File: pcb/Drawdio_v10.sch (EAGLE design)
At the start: 14 parts, among them IC1 TLC551, Q1 BC327

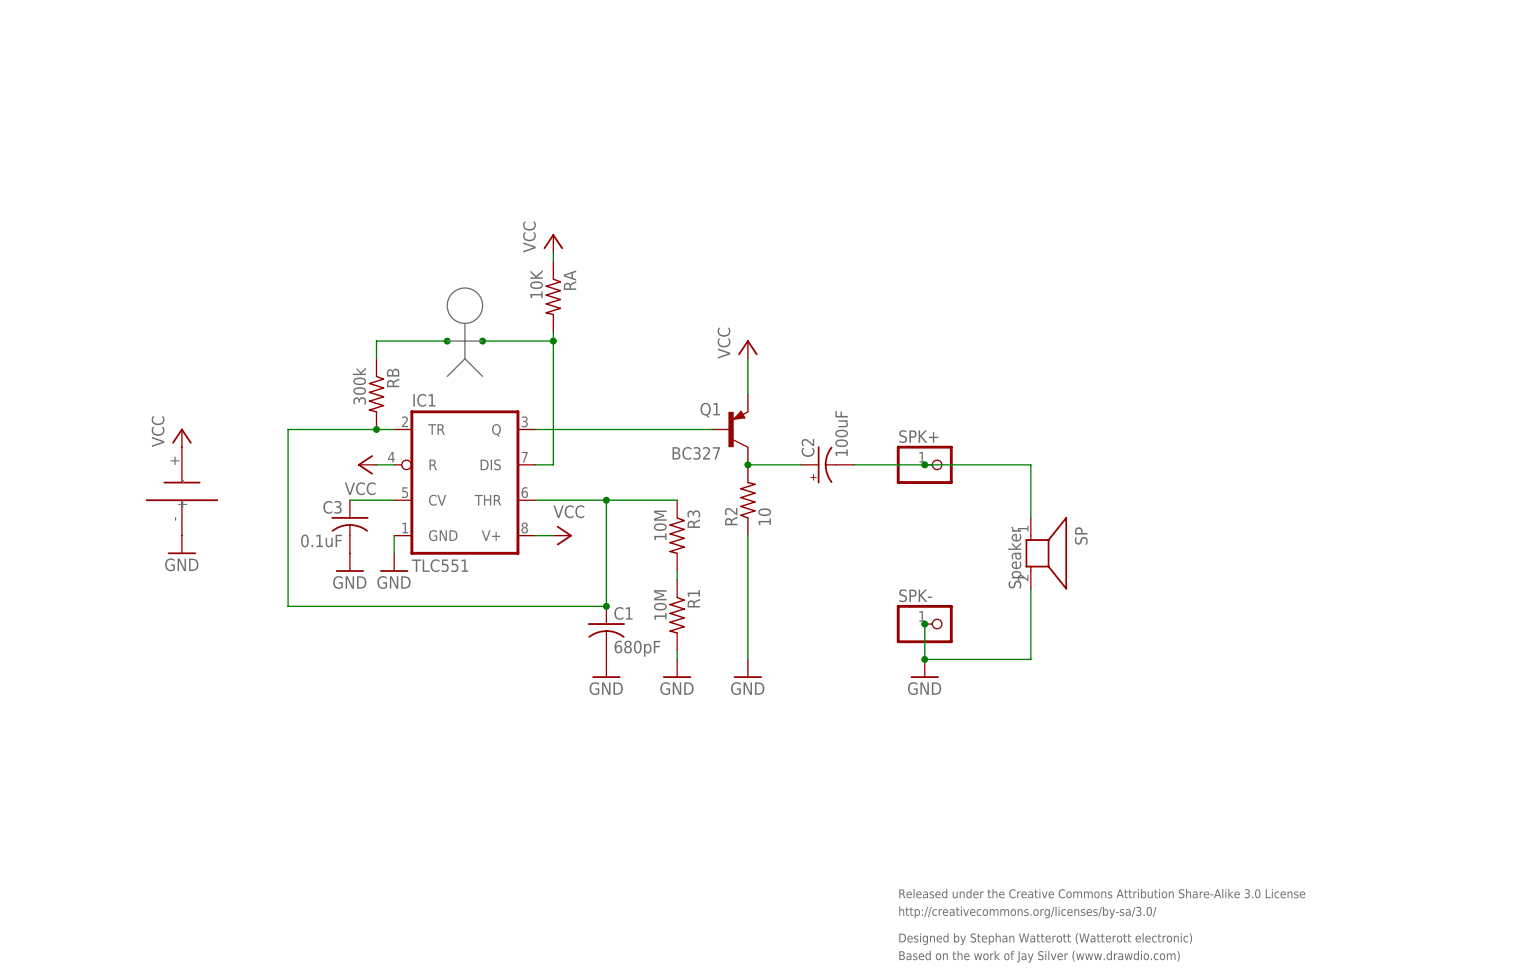
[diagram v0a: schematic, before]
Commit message: updated schematics
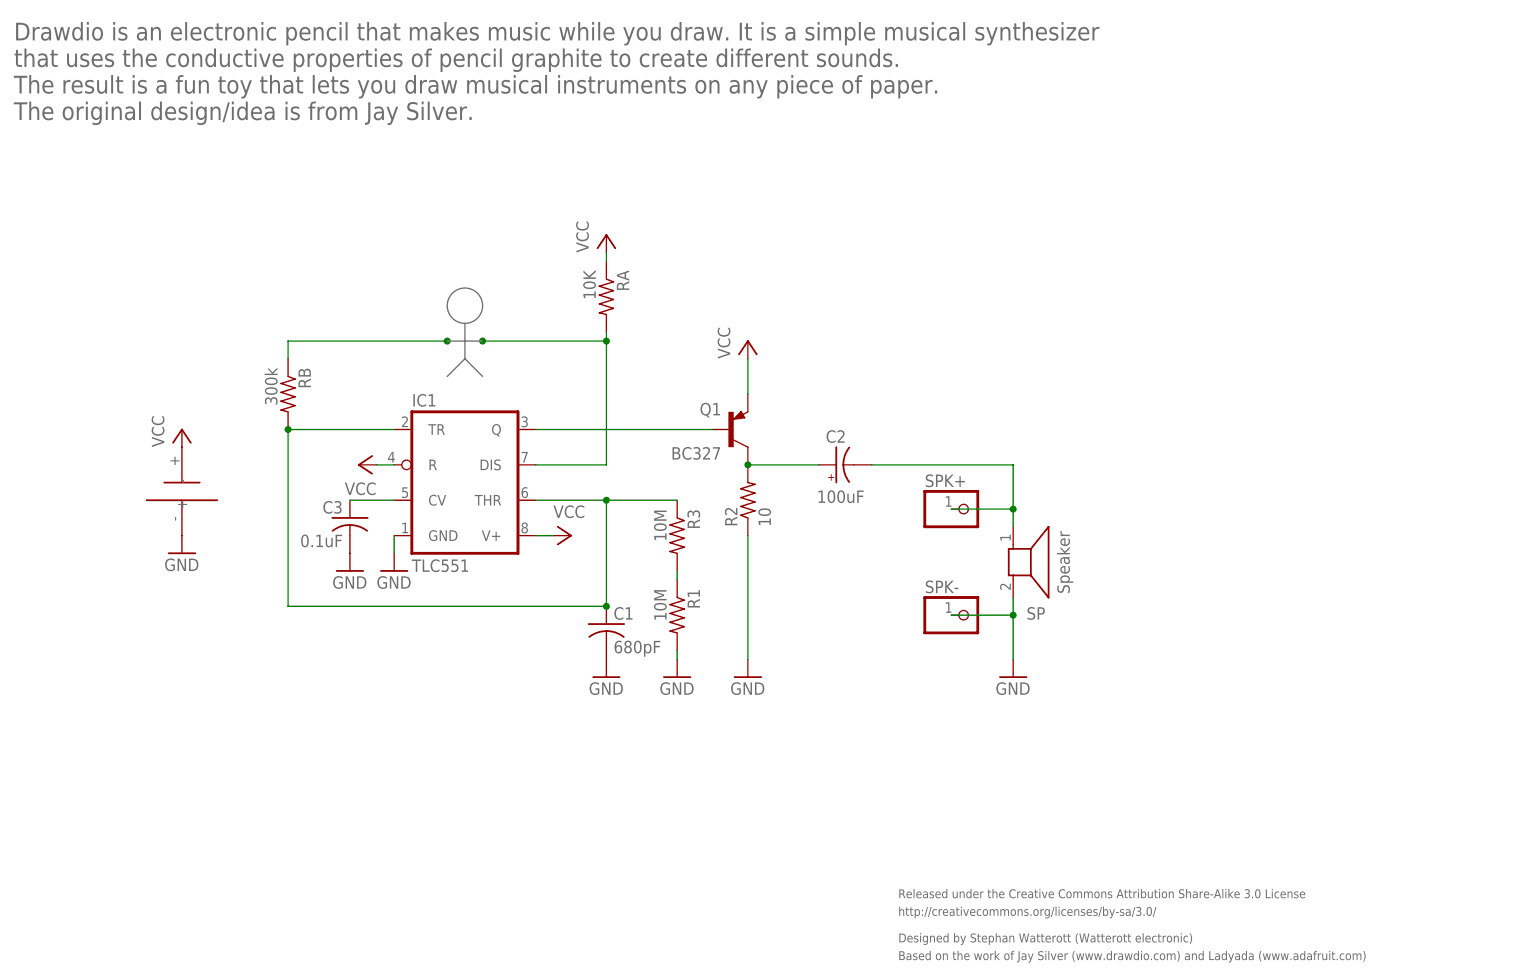
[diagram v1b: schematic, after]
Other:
- note added: "Based on the work of Jay Silver (www.drawdio.com) and Ladyada (www.adafruit.com)"
- note added: "Drawdio is an electronic pencil that makes music while you draw. It is a simple musical synthesizer that uses the conductive properties of pencil graphite to create different sounds. The result is a fun toy that lets you draw musical instruments on any piece of paper. The original design/idea is from Jay Silver."
- note removed: "Based on the work of Jay Silver (www.drawdio.com)"
- moved on the sheet: C2, RA, RB, SP, SPK+, SPK-
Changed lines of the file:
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@@
 <text x="161.29" y="31.75" size="1.27" layer="95">http://creativecommons.org/licenses/by-sa/3.0/</text>
 <text x="161.29" y="27.94" size="1.27" layer="95">Designed by Stephan Watterott (Watterott electronic)</text>
-<text x="161.29" y="25.4" size="1.27" layer="95">Based on the work of Jay Silver (www.drawdio.com)</text>
+<text x="161.29" y="25.4" size="1.27" layer="95">Based on the work of Jay Silver (www.drawdio.com) and Ladyada (www.adafruit.com)</text>
+<text x="34.29" y="146.05" size="2.54" layer="95">Drawdio is an electronic pencil that makes music while you draw. It is a simple musical synthesizer
+that uses the conductive properties of pencil graphite to create different sounds.
+The result is a fun toy that lets you draw musical instruments on any piece of paper.
+The original design/idea is from Jay Silver.</text>
 </plain>
 <instances>
@@
 <instance part="C3" gate="G$1" x="82.55" y="88.9" rot="MR0"/>
 <instance part="P+3" gate="VCC" x="114.3" y="86.36" rot="R270"/>
-<instance part="RB" gate="G$1" x="86.36" y="106.68" rot="R270"/>
+<instance part="RB" gate="G$1" x="73.66" y="106.68" rot="R270"/>
 <instance part="C1" gate="G$1" x="119.38" y="73.66"/>
-<instance part="RA" gate="G$1" x="111.76" y="120.65" rot="R270"/>
-<instance part="P+5" gate="VCC" x="111.76" y="129.54"/>
+<instance part="RA" gate="G$1" x="119.38" y="120.65" rot="R270"/>
+<instance part="P+5" gate="VCC" x="119.38" y="129.54"/>
 <instance part="P+6" gate="VCC" x="139.7" y="114.3"/>
-<instance part="C2" gate="G$1" x="149.86" y="96.52" smashed="yes" rot="R90">
-<attribute name="NAME" x="149.225" y="97.536" size="1.778" layer="95" rot="R90"/>
-<attribute name="VALUE" x="154.051" y="97.536" size="1.778" layer="96" rot="R90"/>
+<instance part="C2" gate="G$1" x="152.4" y="96.52" smashed="yes" rot="R90">
+<attribute name="NAME" x="150.876" y="99.695" size="1.778" layer="95"/>
+<attribute name="VALUE" x="149.606" y="91.059" size="1.778" layer="96"/>
 </instance>
 <instance part="P+7" gate="VCC" x="58.42" y="101.6"/>
-<instance part="SPK+" gate="G$1" x="167.64" y="96.52"/>
-<instance part="SPK-" gate="G$1" x="167.64" y="73.66"/>
+<instance part="SPK+" gate="G$1" x="171.45" y="90.17"/>
+<instance part="SPK-" gate="G$1" x="171.45" y="74.93"/>
 <instance part="GND1" gate="1" x="58.42" y="83.82"/>
 <instance part="GND3" gate="1" x="88.9" y="81.28"/>
@@
 <instance part="GND5" gate="1" x="119.38" y="66.04"/>
 <instance part="GND6" gate="1" x="139.7" y="66.04"/>
-<instance part="GND7" gate="1" x="165.1" y="66.04"/>
+<instance part="GND7" gate="1" x="177.8" y="66.04"/>
 <instance part="R1" gate="G$1" x="129.54" y="74.93" rot="R270"/>
 <instance part="R2" gate="G$1" x="139.7" y="91.44" rot="R90"/>
 <instance part="IC1" gate="A" x="99.06" y="93.98"/>
-<instance part="SP" gate="G$1" x="180.34" y="83.82" rot="R270"/>
+<instance part="SP" gate="G$1" x="177.8" y="82.55" smashed="yes" rot="R270">
+<attribute name="NAME" x="179.705" y="74.295" size="1.778" layer="95"/>
+<attribute name="VALUE" x="184.15" y="86.995" size="1.778" layer="96" rot="R270"/>
+</instance>
 <instance part="Q1" gate="G$1" x="137.16" y="101.6" smashed="yes">
 <attribute name="NAME" x="135.89" y="105.41" size="1.778" layer="95" rot="R180"/>
@@
 <pinref part="RA" gate="G$1" pin="1"/>
 <pinref part="P+5" gate="VCC" pin="VCC"/>
-<wire x1="111.76" y1="125.73" x2="111.76" y2="127" width="0.1524" layer="91"/>
+<wire x1="119.38" y1="125.73" x2="119.38" y2="127" width="0.1524" layer="91"/>
 </segment>
 <segment>
@@
 <net name="N$5" class="0">
 <segment>
-<wire x1="86.36" y1="111.76" x2="86.36" y2="114.3" width="0.1524" layer="91"/>
-<wire x1="86.36" y1="114.3" x2="96.52" y2="114.3" width="0.1524" layer="91"/>
+<wire x1="73.66" y1="111.76" x2="73.66" y2="114.3" width="0.1524" layer="91"/>
+<wire x1="73.66" y1="114.3" x2="96.52" y2="114.3" width="0.1524" layer="91"/>
 <junction x="96.52" y="114.3"/>
 <pinref part="RB" gate="G$1" pin="1"/>
@@
 <net name="N$6" class="0">
 <segment>
-<wire x1="101.6" y1="114.3" x2="111.76" y2="114.3" width="0.1524" layer="91"/>
-<wire x1="111.76" y1="114.3" x2="111.76" y2="96.52" width="0.1524" layer="91"/>
-<wire x1="111.76" y1="96.52" x2="109.22" y2="96.52" width="0.1524" layer="91"/>
-<wire x1="111.76" y1="115.57" x2="111.76" y2="114.3" width="0.1524" layer="91"/>
-<junction x="111.76" y="114.3"/>
+<wire x1="101.6" y1="114.3" x2="119.38" y2="114.3" width="0.1524" layer="91"/>
+<wire x1="119.38" y1="114.3" x2="119.38" y2="96.52" width="0.1524" layer="91"/>
+<wire x1="119.38" y1="96.52" x2="109.22" y2="96.52" width="0.1524" layer="91"/>
+<wire x1="119.38" y1="115.57" x2="119.38" y2="114.3" width="0.1524" layer="91"/>
+<junction x="119.38" y="114.3"/>
 <junction x="101.6" y="114.3"/>
 <pinref part="RA" gate="G$1" pin="2"/>
@@
 <net name="N$3" class="0">
 <segment>
-<wire x1="147.32" y1="96.52" x2="139.7" y2="96.52" width="0.1524" layer="91"/>
+<wire x1="149.86" y1="96.52" x2="139.7" y2="96.52" width="0.1524" layer="91"/>
 <junction x="139.7" y="96.52"/>
 <pinref part="C2" gate="G$1" pin="+"/>
@@
 <net name="N$7" class="0">
 <segment>
-<wire x1="165.1" y1="96.52" x2="154.94" y2="96.52" width="0.1524" layer="91"/>
-<wire x1="180.34" y1="88.9" x2="180.34" y2="96.52" width="0.1524" layer="91"/>
-<wire x1="180.34" y1="96.52" x2="165.1" y2="96.52" width="0.1524" layer="91"/>
-<junction x="165.1" y="96.52"/>
+<wire x1="177.8" y1="96.52" x2="157.48" y2="96.52" width="0.1524" layer="91"/>
+<wire x1="177.8" y1="87.63" x2="177.8" y2="90.17" width="0.1524" layer="91"/>
+<wire x1="177.8" y1="96.52" x2="177.8" y2="90.17" width="0.1524" layer="91"/>
+<wire x1="177.8" y1="90.17" x2="168.91" y2="90.17" width="0.1524" layer="91"/>
 <pinref part="C2" gate="G$1" pin="-"/>
 <pinref part="SPK+" gate="G$1" pin="1"/>
 <pinref part="SP" gate="G$1" pin="1"/>
+<junction x="177.8" y="90.17"/>
 </segment>
 </net>
@@
 </segment>
 <segment>
-<wire x1="180.34" y1="78.74" x2="180.34" y2="68.58" width="0.1524" layer="91"/>
-<wire x1="180.34" y1="68.58" x2="165.1" y2="68.58" width="0.1524" layer="91"/>
-<wire x1="165.1" y1="68.58" x2="165.1" y2="73.66" width="0.1524" layer="91"/>
-<junction x="165.1" y="68.58"/>
-<junction x="165.1" y="73.66"/>
+<wire x1="177.8" y1="77.47" x2="177.8" y2="74.93" width="0.1524" layer="91"/>
+<wire x1="177.8" y1="68.58" x2="177.8" y2="74.93" width="0.1524" layer="91"/>
+<wire x1="177.8" y1="74.93" x2="168.91" y2="74.93" width="0.1524" layer="91"/>
 <pinref part="SPK-" gate="G$1" pin="1"/>
 <pinref part="GND7" gate="1" pin="GND"/>
 <pinref part="SP" gate="G$1" pin="2"/>
+<junction x="177.8" y="74.93"/>
 </segment>
 <segment>
@@
 <net name="N$4" class="0">
 <segment>
-<wire x1="88.9" y1="101.6" x2="86.36" y2="101.6" width="0.1524" layer="91"/>
-<wire x1="86.36" y1="101.6" x2="73.66" y2="101.6" width="0.1524" layer="91"/>
+<wire x1="88.9" y1="101.6" x2="73.66" y2="101.6" width="0.1524" layer="91"/>
 <wire x1="73.66" y1="101.6" x2="73.66" y2="76.2" width="0.1524" layer="91"/>
 <wire x1="73.66" y1="76.2" x2="119.38" y2="76.2" width="0.1524" layer="91"/>
 <wire x1="109.22" y1="91.44" x2="119.38" y2="91.44" width="0.1524" layer="91"/>
 <wire x1="119.38" y1="91.44" x2="119.38" y2="76.2" width="0.1524" layer="91"/>
-<junction x="86.36" y="101.6"/>
+<junction x="73.66" y="101.6"/>
 <junction x="119.38" y="76.2"/>
 <pinref part="RB" gate="G$1" pin="2"/>
@@
 </schematic>
 </drawing>
+<compatibility>
+<note version="6.3" minversion="6.2.2" severity="warning">
+Since Version 6.2.2 text objects can contain more than one line,
+which will not be processed correctly with this version.
+</note>
+</compatibility>
 </eagle>

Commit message: updated license information
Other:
- note added: "Released under the Creative Commons Attribution Share-Alike License"
- note added: "http://creativecommons.org/licenses/by-sa/4.0/"
- note removed: "Released under the Creative Commons Attribution Share-Alike 3.0 License"
- note removed: "http://creativecommons.org/licenses/by-sa/3.0/"
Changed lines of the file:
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@@
 <setting verticaltext="up"/>
 </settings>
-<grid distance="0.05" unitdist="inch" unit="inch" style="lines" multiple="1" display="yes" altdistance="0.025" altunitdist="inch" altunit="inch"/>
+<grid distance="0.1" unitdist="inch" unit="inch" style="lines" multiple="1" display="no" altdistance="0.01" altunitdist="inch" altunit="inch"/>
 <layers>
 <layer number="1" name="Top" color="4" fill="1" visible="no" active="no"/>
@@
 <wire x1="96.52" y1="114.3" x2="101.6" y2="114.3" width="0.1524" layer="95"/>
 <circle x="99.06" y="119.38" radius="2.54" width="0.1524" layer="95"/>
-<text x="161.29" y="34.29" size="1.27" layer="95">Released under the Creative Commons Attribution Share-Alike 3.0 License</text>
-<text x="161.29" y="31.75" size="1.27" layer="95">http://creativecommons.org/licenses/by-sa/3.0/</text>
+<text x="161.29" y="34.29" size="1.27" layer="95">Released under the Creative Commons Attribution Share-Alike License</text>
+<text x="161.29" y="31.75" size="1.27" layer="95">http://creativecommons.org/licenses/by-sa/4.0/</text>
 <text x="161.29" y="27.94" size="1.27" layer="95">Designed by Stephan Watterott (Watterott electronic)</text>
 <text x="161.29" y="25.4" size="1.27" layer="95">Based on the work of Jay Silver (www.drawdio.com) and Ladyada (www.adafruit.com)</text>
